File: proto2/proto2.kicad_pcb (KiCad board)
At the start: 2 copper layers, 205.2 x 110 mm, 219 parts, among them J1 Output 1, J10 Output, J11 Device, J12 Daughter Card, J2 Main Power, J3 Output, J4 Output, J5 Device, J6 Output, J7 Device, J8 Output, J9 Device, Q1 2N7002, Q10 2N7002, Q11 2N7002, Q12 2N7002, Q2 2N7002, Q3 2N7002, Q4 2N7002, Q5 2N7002, Q6 2N7002, Q7 2N7002, Q8 2N7002, Q9 2N7002, SW1 SW_DIP_x04, U1 AQY282SX, U10 AQY282SX, U11 AQY282SX, U12 AQY282SX, U13 NCP59300, U2 AQY282SX, U3 AQY282SX, U4 AQY282SX, U5 AQY282SX, U6 AQY282SX, U7 AQY282SX, U8 AQY282SX, U9 AQY282SX

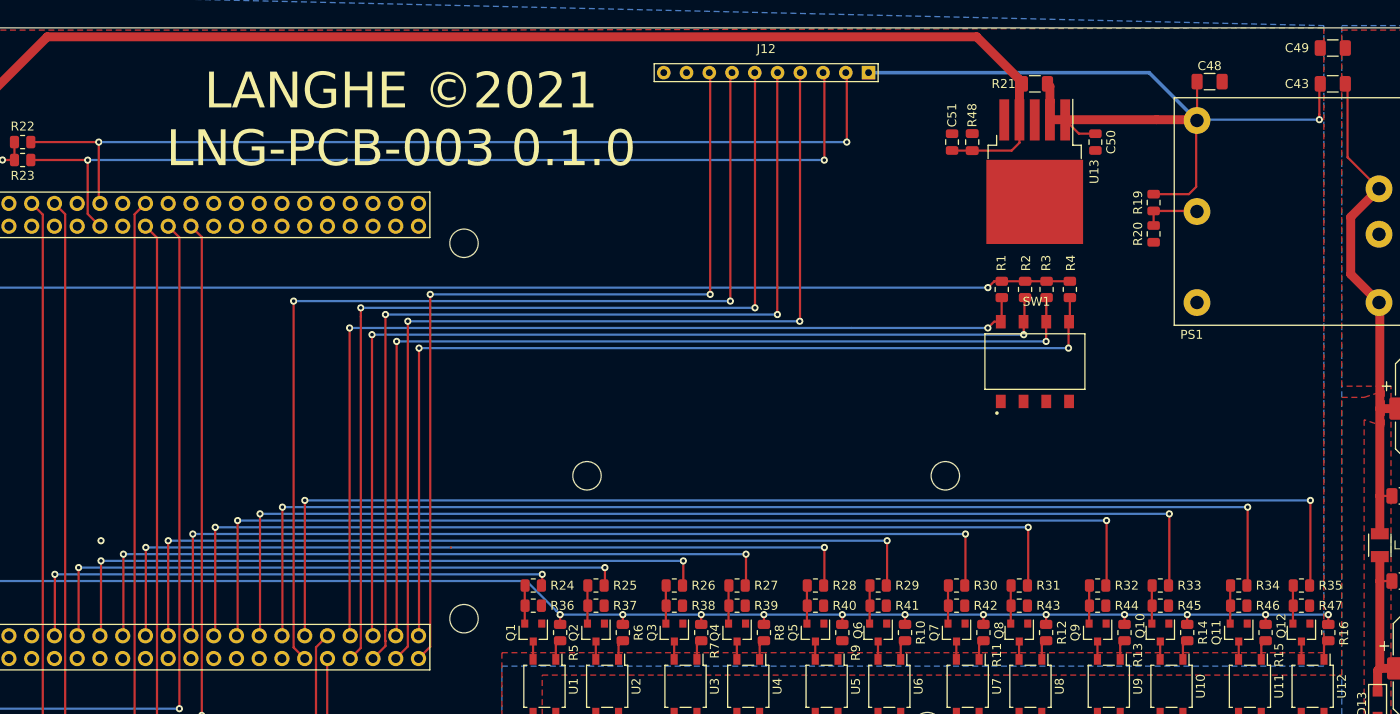
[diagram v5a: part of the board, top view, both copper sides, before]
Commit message: Replaced 2N7000 symbol with 2N7002.
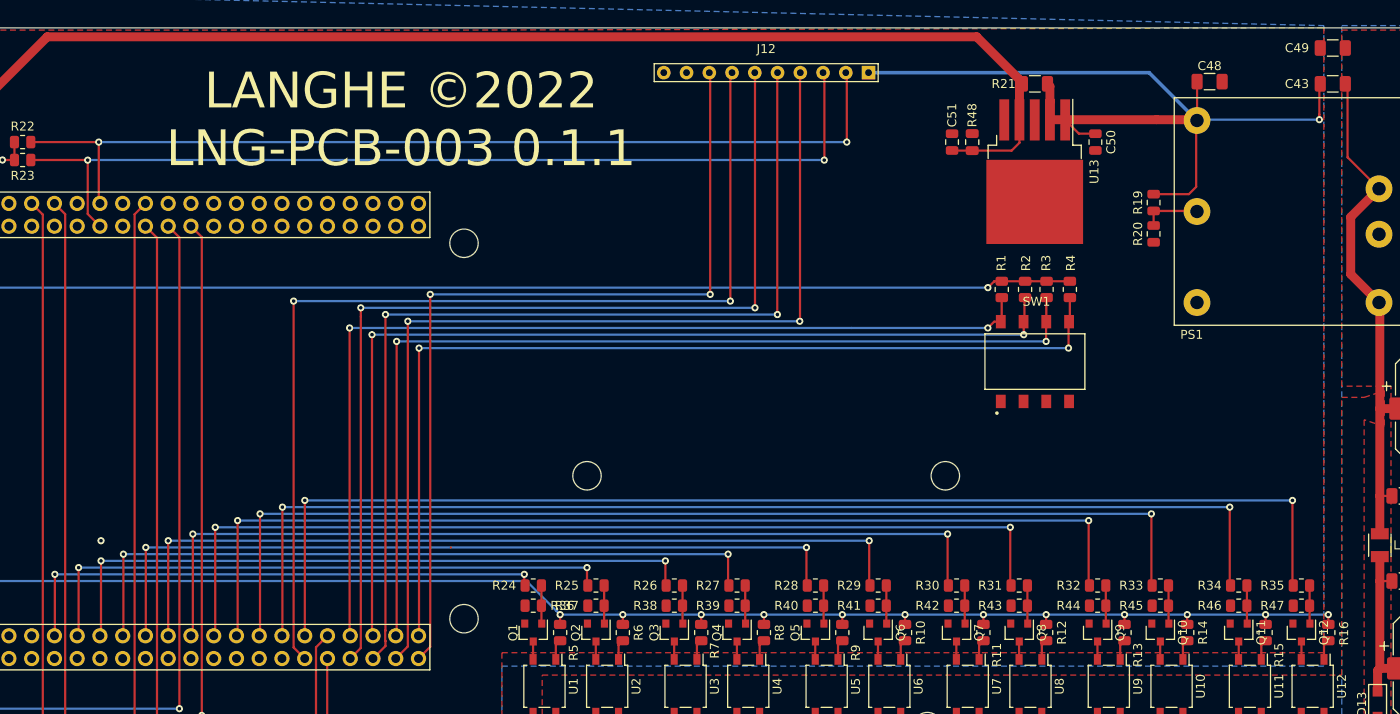
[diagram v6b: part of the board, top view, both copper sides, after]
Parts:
- turned R24 to 180 degrees
- turned R25 to 180 degrees
- turned R26 to 180 degrees
- turned R27 to 180 degrees
- turned R28 to 180 degrees
- turned R29 to 180 degrees
- turned R30 to 180 degrees
- turned R31 to 180 degrees
- turned R32 to 180 degrees
- turned R33 to 180 degrees
- turned R34 to 180 degrees
- turned R35 to 180 degrees
- turned R36 to 180 degrees
- turned R37 to 180 degrees
- turned R38 to 180 degrees
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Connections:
- Q1 pad 1: GND -> Net-(Q1-Pad1)
- Q1 pad 2: Net-(Q1-Pad2) -> GND
- Q10 pad 1: GND -> Net-(Q10-Pad1)
- Q10 pad 2: Net-(Q10-Pad2) -> GND
- Q11 pad 1: GND -> Net-(Q11-Pad1)
- Q11 pad 2: Net-(Q11-Pad2) -> GND
- Q12 pad 1: GND -> Net-(Q12-Pad1)
- Q12 pad 2: Net-(Q12-Pad2) -> GND
- Q2 pad 1: GND -> Net-(Q2-Pad1)
- Q2 pad 2: Net-(Q2-Pad2) -> GND
- Q3 pad 1: GND -> Net-(Q3-Pad1)
- Q3 pad 2: Net-(Q3-Pad2) -> GND
- Q4 pad 1: GND -> Net-(Q4-Pad1)
- Q4 pad 2: Net-(Q4-Pad2) -> GND
- Q5 pad 1: GND -> Net-(Q5-Pad1)
- Q5 pad 2: Net-(Q5-Pad2) -> GND
- Q6 pad 1: GND -> Net-(Q6-Pad1)
- Q6 pad 2: Net-(Q6-Pad2) -> GND
- Q7 pad 1: GND -> Net-(Q7-Pad1)
- Q7 pad 2: Net-(Q7-Pad2) -> GND
- Q8 pad 1: GND -> Net-(Q8-Pad1)
- Q8 pad 2: Net-(Q8-Pad2) -> GND
- Q9 pad 1: GND -> Net-(Q9-Pad1)
- Q9 pad 2: Net-(Q9-Pad2) -> GND
- R24 pad 1: Net-(Q1-Pad2) -> Net-(Q1-Pad1)
- R25 pad 1: Net-(Q2-Pad2) -> Net-(Q2-Pad1)
- R26 pad 1: Net-(Q3-Pad2) -> Net-(Q3-Pad1)
- R27 pad 1: Net-(Q4-Pad2) -> Net-(Q4-Pad1)
- R28 pad 1: Net-(Q5-Pad2) -> Net-(Q5-Pad1)
- R29 pad 1: Net-(Q6-Pad2) -> Net-(Q6-Pad1)
- R30 pad 1: Net-(Q7-Pad2) -> Net-(Q7-Pad1)
- R31 pad 1: Net-(Q8-Pad2) -> Net-(Q8-Pad1)
- R32 pad 1: Net-(Q9-Pad2) -> Net-(Q9-Pad1)
- R33 pad 1: Net-(Q10-Pad2) -> Net-(Q10-Pad1)
- R34 pad 1: Net-(Q11-Pad2) -> Net-(Q11-Pad1)
- R35 pad 1: Net-(Q12-Pad2) -> Net-(Q12-Pad1)
- R36 pad 1: Net-(Q1-Pad2) -> Net-(Q1-Pad1)
- R37 pad 1: Net-(Q2-Pad2) -> Net-(Q2-Pad1)
- R38 pad 1: Net-(Q3-Pad2) -> Net-(Q3-Pad1)
- R39 pad 1: Net-(Q4-Pad2) -> Net-(Q4-Pad1)
- R40 pad 1: Net-(Q5-Pad2) -> Net-(Q5-Pad1)
- R41 pad 1: Net-(Q6-Pad2) -> Net-(Q6-Pad1)
- R42 pad 1: Net-(Q7-Pad2) -> Net-(Q7-Pad1)
- R43 pad 1: Net-(Q8-Pad2) -> Net-(Q8-Pad1)
- R44 pad 1: Net-(Q9-Pad2) -> Net-(Q9-Pad1)
- R45 pad 1: Net-(Q10-Pad2) -> Net-(Q10-Pad1)
- R46 pad 1: Net-(Q11-Pad2) -> Net-(Q11-Pad1)
- R47 pad 1: Net-(Q12-Pad2) -> Net-(Q12-Pad1)
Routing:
- net Net-(Q10-Pad1): track 0.00 -> 4.51 mm
- net Net-(Q1-Pad1): track 0.00 -> 4.48 mm
- net Net-(Q2-Pad1): track 0.00 -> 4.39 mm
- net Net-(Q9-Pad1): track 0.00 -> 4.39 mm
- net Net-(Q8-Pad1): track 0.00 -> 4.39 mm
- net Net-(Q7-Pad1): track 0.00 -> 4.39 mm
- net Net-(Q6-Pad1): track 0.00 -> 4.39 mm
- net Net-(Q5-Pad1): track 0.00 -> 4.39 mm
- net Net-(Q4-Pad1): track 0.00 -> 4.39 mm
- net Net-(Q3-Pad1): track 0.00 -> 4.39 mm
- net Net-(Q12-Pad1): track 0.00 -> 4.39 mm
- net Net-(Q11-Pad1): track 0.00 -> 4.39 mm
- net Net-(Q2-Pad2): track 4.27 -> 0.00 mm
- net Net-(Q8-Pad2): track 4.27 -> 0.00 mm
- net Net-(Q6-Pad2): track 4.27 -> 0.00 mm
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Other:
- board text added: "LANGHE ©2022 LNG-PCB-003 0.1.1"
- board text removed: "LANGHE ©2021 LNG-PCB-003 0.1.0"

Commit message: Replaces board outline with Polycase DC-96 outline.
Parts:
- removed MH1, MH3: Conn_01x01, STD-xxx:NPTH-.125
- removed MH2, MH4: Conn_01x01, STD-xxx:STD-.125_wide
- added REF**: Polycase_DC96, BCR_Langhe:Polycase_DC96, F.Cu at (112.8, 113.2)
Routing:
- net +5V: track 538.7 -> 494.3 mm
- net GND: vias 4 -> 3
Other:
- board size 205.2 x 110 mm -> 245.9 x 144.3 mm

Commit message: Added another 2 outputs and re-routed board.
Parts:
- added C54: 10uF, Capacitor_SMD:C_0805_2012Metric, F.Cu at (196.8, 146.0)
- added C55: 10uF, Capacitor_SMD:C_0805_2012Metric, F.Cu at (200.2, 144.0)
- added C56: 10uF, Capacitor_SMD:C_0805_2012Metric, F.Cu at (203.8, 146.0)
- added C57: 10uF, Capacitor_SMD:C_0805_2012Metric, F.Cu at (207.2, 144.0)
- added D13: D_Small_ALT, Diode_SMD:D_SOD-123F, F.Cu at (199.5, 148.2)
- added D14: D_Small_ALT, Diode_SMD:D_SOD-123F, F.Cu at (206.5, 148.2)
- added F13: 0.5A, Resistor_SMD:R_1206_3216Metric, F.Cu at (197.8, 133.2)
- added F14: 0.5A, Resistor_SMD:R_1206_3216Metric, F.Cu at (204.8, 133.2)
- added J12: Output, Connector_BCR:Phoenix_Contact_PST_4, F.Cu at (203.0, 152.5)
- added L44: 1A Ferrite, Resistor_SMD:R_1206_3216Metric, F.Cu at (197.8, 139.2)
- added L45: 1A Ferrite, Resistor_SMD:R_1206_3216Metric, F.Cu at (201.2, 139.2)
- added L46: 1A Ferrite, Resistor_SMD:R_1206_3216Metric, F.Cu at (204.8, 139.2)
- added L47: 1A Ferrite, Resistor_SMD:R_1206_3216Metric, F.Cu at (208.2, 139.2)
- added Q13: 2N7002, Package_BCR:SOT-23, F.Cu at (197.8, 120.5)
- added Q14: 2N7002, Package_BCR:SOT-23, F.Cu at (204.8, 120.5)
- added R17: 433R, Resistor_SMD:R_0805_2012Metric, F.Cu at (200.8, 120.5)
- added R18: 433R, Resistor_SMD:R_0805_2012Metric, F.Cu at (207.8, 120.5)
- added R48: 27K, Resistor_SMD:R_0805_2012Metric, F.Cu at (197.8, 117.5)
- added R49: 27K, Resistor_SMD:R_0805_2012Metric, F.Cu at (204.8, 117.5)
- added R50: 1K, Resistor_SMD:R_0805_2012Metric, F.Cu at (197.8, 115.2)
- added R51: 1K, Resistor_SMD:R_0805_2012Metric, F.Cu at (204.8, 115.2)
- added U13: AQY282SX, Package_SO:SO-4_4.4x4.3mm_P2.54mm, F.Cu at (199.0, 126.5)
- added U14: AQY282SX, Package_SO:SO-4_4.4x4.3mm_P2.54mm, F.Cu at (206.0, 126.5)
- C16, C17, C24, C25, C32, C33, C40, C41: value 10uF -> DNP
- L16, L17, L24, L25, L32, L33, L40, L41: value 500mA Ferrite -> 0R
- moved C52 38.8 mm to (-1.75, 142.5)
- moved R52 38.8 mm to (-5.50, 142.5)
- moved L37 15.8 mm to (189.0, 139.2)
- moved L38 15.8 mm to (192.5, 139.2)
- moved C1 15.8 mm to (102.2, 146.0)
- moved C10 15.8 mm to (128.5, 144.0)
- moved C11 15.8 mm to (133.8, 146.0)
- moved C12 15.8 mm to (137.2, 144.0)
- moved C13 15.8 mm to (140.8, 146.0)
- moved C14 15.8 mm to (144.2, 144.0)
- moved C15 15.8 mm to (38.5, 147.2)
- moved C16 15.8 mm to (35.0, 147.2)
- moved C17 15.8 mm to (31.5, 147.2)
- moved C18 15.8 mm to (28.0, 147.2)
- moved C19 15.8 mm to (149.5, 146.0)
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- renumbered D13 to D15, F13 to F15, F14 to F16, F15 to F17, F16 to F18, F17 to F19, J12 to J13, R17 to R52, R18 to R53, R48 to R54, U13 to U15
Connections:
- net VDQ1 renamed +24V
- BB1 pad 8.10: Net-(BB1-Pad8.10) -> unconnected-(BB1-Pad8.10)
- BB1 pad 8.11: Net-(BB1-Pad8.11) -> unconnected-(BB1-Pad8.11)
- BB1 pad 8.12: Net-(BB1-Pad8.12) -> unconnected-(BB1-Pad8.12)
- BB1 pad 8.13: OUT_1 -> unconnected-(BB1-Pad8.13)
- BB1 pad 8.14: Net-(BB1-Pad8.14) -> OUT_1
- BB1 pad 8.15: OUT_2 -> unconnected-(BB1-Pad8.15)
- BB1 pad 8.16: Net-(BB1-Pad8.16) -> OUT_2
- BB1 pad 8.17: OUT_3 -> unconnected-(BB1-Pad8.17)
- BB1 pad 8.18: Net-(BB1-Pad8.18) -> OUT_3
- BB1 pad 8.19: OUT_4 -> unconnected-(BB1-Pad8.19)
- BB1 pad 8.20: Net-(BB1-Pad8.20) -> OUT_4
- BB1 pad 8.22: Net-(BB1-Pad8.22) -> unconnected-(BB1-Pad8.22)
- BB1 pad 8.24: Net-(BB1-Pad8.24) -> unconnected-(BB1-Pad8.24)
- BB1 pad 8.26: Net-(BB1-Pad8.26) -> unconnected-(BB1-Pad8.26)
- BB1 pad 8.28: Net-(BB1-Pad8.28) -> unconnected-(BB1-Pad8.28)
- BB1 pad 8.3: Net-(BB1-Pad8.3) -> unconnected-(BB1-Pad8.3)
- BB1 pad 8.30: Net-(BB1-Pad8.30) -> unconnected-(BB1-Pad8.30)
- BB1 pad 8.32: Net-(BB1-Pad8.32) -> unconnected-(BB1-Pad8.32)
- BB1 pad 8.34: Net-(BB1-Pad8.34) -> unconnected-(BB1-Pad8.34)
- BB1 pad 8.36: GP_4 -> unconnected-(BB1-Pad8.36)
- BB1 pad 8.39: BS_1 -> OUT_13
- BB1 pad 8.4: Net-(BB1-Pad8.4) -> unconnected-(BB1-Pad8.4)
- BB1 pad 8.40: GP_3 -> BS_4
- BB1 pad 8.41: BS_2 -> OUT_14
- BB1 pad 8.42: GP_2 -> BS_3
- BB1 pad 8.43: BS_3 -> unconnected-(BB1-Pad8.43)
- BB1 pad 8.44: GP_1 -> BS_2
- BB1 pad 8.45: BS_4 -> unconnected-(BB1-Pad8.45)
- BB1 pad 8.46: BS_5 -> BS_1
- BB1 pad 8.5: Net-(BB1-Pad8.5) -> unconnected-(BB1-Pad8.5)
- BB1 pad 8.6: Net-(BB1-Pad8.6) -> unconnected-(BB1-Pad8.6)
- BB1 pad 8.7: Net-(BB1-Pad8.7) -> unconnected-(BB1-Pad8.7)
- BB1 pad 8.8: +5V -> unconnected-(BB1-Pad8.8)
- BB1 pad 8.9: Net-(BB1-Pad8.9) -> unconnected-(BB1-Pad8.9)
- BB1 pad 9.10: Net-(BB1-Pad9.10) -> unconnected-(BB1-Pad9.10)
- BB1 pad 9.12: Net-(BB1-Pad9.12) -> unconnected-(BB1-Pad9.12)
- BB1 pad 9.14: Net-(BB1-Pad9.14) -> unconnected-(BB1-Pad9.14)
- BB1 pad 9.15: Net-(BB1-Pad9.15) -> unconnected-(BB1-Pad9.15)
- BB1 pad 9.16: Net-(BB1-Pad9.16) -> unconnected-(BB1-Pad9.16)
- BB1 pad 9.19: Net-(BB1-Pad9.19) -> unconnected-(BB1-Pad9.19)
- BB1 pad 9.20: Net-(BB1-Pad9.20) -> unconnected-(BB1-Pad9.20)
- BB1 pad 9.23: Net-(BB1-Pad9.23) -> GP_1
- BB1 pad 9.25: Net-(BB1-Pad9.25) -> GP_2
- BB1 pad 9.27: Net-(BB1-Pad9.27) -> GP_3
- BB1 pad 9.28: Net-(BB1-Pad9.28) -> unconnected-(BB1-Pad9.28)
- BB1 pad 9.29: Net-(BB1-Pad9.29) -> GP_4
- BB1 pad 9.30: Net-(BB1-Pad9.30) -> unconnected-(BB1-Pad9.30)
- BB1 pad 9.31: Net-(BB1-Pad9.31) -> BS_5
- BB1 pad 9.32: Net-(BB1-Pad9.32) -> unconnected-(BB1-Pad9.32)
- BB1 pad 9.33: Net-(BB1-Pad9.33) -> unconnected-(BB1-Pad9.33)
- BB1 pad 9.34: Net-(BB1-Pad9.34) -> unconnected-(BB1-Pad9.34)
- BB1 pad 9.35: Net-(BB1-Pad9.35) -> unconnected-(BB1-Pad9.35)
- BB1 pad 9.36: Net-(BB1-Pad9.36) -> unconnected-(BB1-Pad9.36)
- BB1 pad 9.37: Net-(BB1-Pad9.37) -> unconnected-(BB1-Pad9.37)
- BB1 pad 9.38: Net-(BB1-Pad9.38) -> unconnected-(BB1-Pad9.38)
- BB1 pad 9.39: Net-(BB1-Pad9.39) -> unconnected-(BB1-Pad9.39)
- BB1 pad 9.40: Net-(BB1-Pad9.40) -> unconnected-(BB1-Pad9.40)
- BB1 pad 9.41: Net-(BB1-Pad9.41) -> unconnected-(BB1-Pad9.41)
- BB1 pad 9.42: Net-(BB1-Pad9.42) -> unconnected-(BB1-Pad9.42)
- BB1 pad 9.9: Net-(BB1-Pad9.9) -> unconnected-(BB1-Pad9.9)
- U15 pad 5: Net-(U13-Pad5) -> unconnected-(U15-Pad5)
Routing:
- net OUT_14: track 0.00 -> 136.7 mm, vias 0 -> 2
- net OUT_13: track 0.00 -> 130.7 mm, vias 0 -> 2
- net GP_4: track 114.9 -> 78.3 mm
- net +5V: track 494.3 -> 523.2 mm, vias 17 -> 19
- net GP_2: track 110.0 -> 81.5 mm
- net GP_3: track 110.1 -> 82.2 mm
- net RX_1: track 98.9 -> 123.7 mm
- net TX_1: track 100.0 -> 124.7 mm
- net TX_2: track 78.2 -> 102.9 mm
- net RX_2: track 74.7 -> 98.2 mm
- net OUT_4: track 80.2 -> 57.7 mm
- net BS_5: track 97.2 -> 75.1 mm
- net OUT_3: track 74.2 -> 52.1 mm
- net GP_1: track 109.7 -> 87.9 mm
- net OUT_2: track 66.5 -> 45.0 mm
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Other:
- board size 245.9 x 144.3 mm -> 245.9 x 132.5 mm
- net class Default removed
